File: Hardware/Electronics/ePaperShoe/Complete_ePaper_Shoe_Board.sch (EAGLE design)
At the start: 59 parts, among them Q1 IRF7509, U1 LM3671MF-3.3/NOPB, U2 NRF52832, U3 MCP73871, X1 32MHz, X2 32.768kHz, X3 FH12-26S-0.5SH

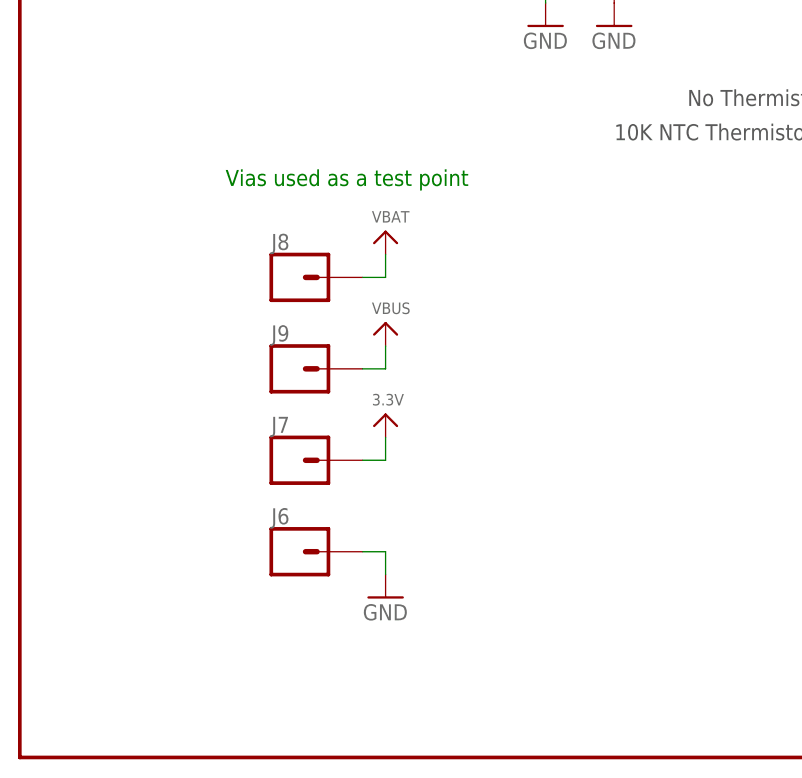
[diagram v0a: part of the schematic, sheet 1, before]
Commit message: Completed layout and traces of PCB. Need to still add silkscreen and arrange lables
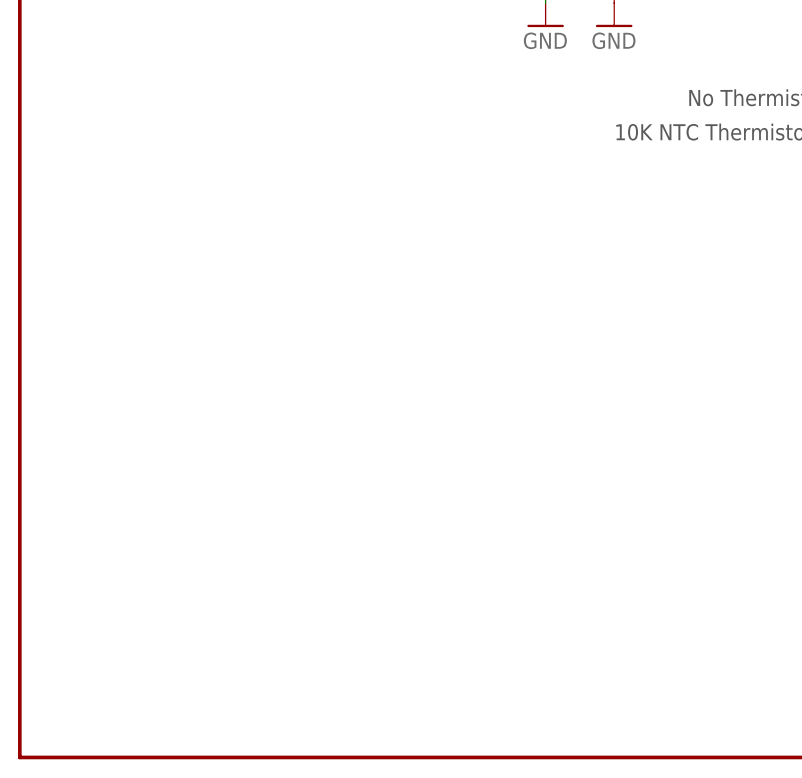
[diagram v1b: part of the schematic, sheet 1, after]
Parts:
- removed J6, J7, J8, J9: (no value), SparkFun-Connectors:CONN_01PTH_NO_SILK_YES_STOP
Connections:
- net 3.3V: no longer J7.1
- net GND: no longer J6.1
- net VBAT: no longer J8.1
- net VBUS: no longer J9.1
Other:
- note removed: "Vias used as a test point"
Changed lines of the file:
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@@
 <part name="R1" library="microbuilder" deviceset="RESISTOR" device="0805" value="100K"/>
 <part name="U$4" library="microbuilder" deviceset="VBAT" device=""/>
-<part name="U$7" library="microbuilder" deviceset="3.3V" device=""/>
-<part name="GND1" library="supply1" library_urn="urn:adsk.eagle:library:371" deviceset="GND" device=""/>
-<part name="U$8" library="microbuilder" deviceset="VBUS" device=""/>
-<part name="U$9" library="microbuilder" deviceset="VBAT" device=""/>
 <part name="FRAME1" library="SparkFun-Aesthetics" deviceset="FRAME-LETTER-MICHAEL" device="NO_PACKAGE"/>
 <part name="UC_LED" library="microbuilder" deviceset="LED" device="0805_NOOUTLINE" value="ORANGE"/>
@@
 <part name="L5" library="microbuilder" deviceset="INDUCTOR" device="NR5040" value="47µH/±30%/420mA"/>
 <part name="J5" library="SparkFun-Connectors" deviceset="CONN_02" device=""/>
-<part name="J6" library="SparkFun-Connectors" deviceset="CONN_01" device="PTH_NO_SILK_YES_STOP"/>
-<part name="J7" library="SparkFun-Connectors" deviceset="CONN_01" device="PTH_NO_SILK_YES_STOP"/>
-<part name="J8" library="SparkFun-Connectors" deviceset="CONN_01" device="PTH_NO_SILK_YES_STOP"/>
-<part name="J9" library="SparkFun-Connectors" deviceset="CONN_01" device="PTH_NO_SILK_YES_STOP"/>
 </parts>
 <sheets>
@@
 <text x="20.32" y="124.46" size="1.778" layer="97" rot="R90">low voltage indicator.</text>
 <text x="185.42" y="86.36" size="1.778" layer="91">5V IN</text>
-<text x="22.86" y="63.5" size="1.778" layer="91">Vias used as a test point</text>
 </plain>
 <instances>
@@
 <instance part="R1" gate="G$1" x="167.64" y="111.76"/>
 <instance part="U$4" gate="G$1" x="152.4" y="119.38"/>
-<instance part="U$7" gate="G$1" x="40.64" y="38.1"/>
-<instance part="GND1" gate="1" x="40.64" y="17.78"/>
-<instance part="U$8" gate="G$1" x="40.64" y="48.26"/>
-<instance part="U$9" gate="G$1" x="40.64" y="58.42"/>
 <instance part="FRAME1" gate="G$1" x="0" y="0"/>
 <instance part="FRAME1" gate="G$2" x="147.32" y="0"/>
 <instance part="J5" gate="G$1" x="187.96" y="91.44"/>
-<instance part="J6" gate="G$1" x="30.48" y="22.86"/>
-<instance part="J7" gate="G$1" x="30.48" y="33.02"/>
-<instance part="J8" gate="G$1" x="30.48" y="53.34"/>
-<instance part="J9" gate="G$1" x="30.48" y="43.18"/>
 </instances>
 <busses>
@@
 <wire x1="203.2" y1="91.44" x2="203.2" y2="78.74" width="0.1524" layer="91"/>
 </segment>
-<segment>
-<pinref part="GND1" gate="1" pin="GND"/>
-<wire x1="38.1" y1="22.86" x2="40.64" y2="22.86" width="0.1524" layer="91"/>
-<wire x1="40.64" y1="22.86" x2="40.64" y2="20.32" width="0.1524" layer="91"/>
-<pinref part="J6" gate="G$1" pin="1"/>
-</segment>
 </net>
 <net name="VBAT" class="0">
@@
 <pinref part="U$4" gate="G$1" pin="VBAT"/>
 <wire x1="152.4" y1="116.84" x2="152.4" y2="111.76" width="0.1524" layer="91"/>
-</segment>
-<segment>
-<pinref part="U$9" gate="G$1" pin="VBAT"/>
-<wire x1="38.1" y1="53.34" x2="40.64" y2="53.34" width="0.1524" layer="91"/>
-<wire x1="40.64" y1="53.34" x2="40.64" y2="55.88" width="0.1524" layer="91"/>
-<pinref part="J8" gate="G$1" pin="1"/>
 </segment>
 </net>
@@
 <pinref part="R6" gate="G$1" pin="2"/>
 </segment>
-<segment>
-<pinref part="U$8" gate="G$1" pin="VBUS"/>
-<wire x1="38.1" y1="43.18" x2="40.64" y2="43.18" width="0.1524" layer="91"/>
-<wire x1="40.64" y1="43.18" x2="40.64" y2="45.72" width="0.1524" layer="91"/>
-<pinref part="J9" gate="G$1" pin="1"/>
-</segment>
 </net>
 <net name="VLIPO" class="0">
@@
 <junction x="236.22" y="134.62"/>
 </segment>
-<segment>
-<pinref part="U$7" gate="G$1" pin="3.3V"/>
-<wire x1="38.1" y1="33.02" x2="40.64" y2="33.02" width="0.1524" layer="91"/>
-<wire x1="40.64" y1="33.02" x2="40.64" y2="35.56" width="0.1524" layer="91"/>
-<pinref part="J7" gate="G$1" pin="1"/>
-</segment>
-</net>
+</net>

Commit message: Changes here and there, refining the product
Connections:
- net GND: now also J5.1
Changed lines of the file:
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@@
 <wire x1="195.58" y1="91.44" x2="203.2" y2="91.44" width="0.1524" layer="91"/>
 <wire x1="203.2" y1="91.44" x2="203.2" y2="78.74" width="0.1524" layer="91"/>
+<pinref part="J5" gate="G$1" pin="1"/>
 </segment>
 </net>
